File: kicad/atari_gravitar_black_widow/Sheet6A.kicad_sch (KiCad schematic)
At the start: 10 parts

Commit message: All digital done!
Need ground flood and analog section.
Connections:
- net PR82: now also H_8.1 (C)
- net ~{LATCH1}: no longer H_8.1 (C)
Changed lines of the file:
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@@
   (junction (at 174.625 68.58) (diameter 0) (color 0 0 0 0)
   )
-  (junction (at 215.265 205.74) (diameter 0) (color 0 0 0 0)
-  )
   (junction (at 384.81 179.705) (diameter 0) (color 0 0 0 0)
   )
@@
   )
   (junction (at 381.635 182.88) (diameter 0) (color 0 0 0 0)
+  )
+  (junction (at 262.255 205.74) (diameter 0) (color 0 0 0 0)
   )
   (junction (at 170.815 55.88) (diameter 0) (color 0 0 0 0)
@@
     (stroke (width 0) (type default) (color 0 0 0 0))
   )
-  (wire (pts (xy 215.265 205.74) (xy 239.395 205.74))
-    (stroke (width 0) (type default) (color 0 0 0 0))
-  )
   (wire (pts (xy 219.075 226.06) (xy 158.115 226.06))
     (stroke (width 0) (type default) (color 0 0 0 0))
@@
     (stroke (width 0) (type default) (color 0 0 0 0))
   )
+  (wire (pts (xy 262.255 205.74) (xy 262.255 208.28))
+    (stroke (width 0) (type default) (color 0 0 0 0))
+  )
   (wire (pts (xy 236.855 203.2) (xy 236.855 198.12))
     (stroke (width 0) (type default) (color 0 0 0 0))
@@
     (stroke (width 0) (type default) (color 0 0 0 0))
   )
-  (wire (pts (xy 215.265 205.74) (xy 215.265 254.635))
+  (wire (pts (xy 215.265 154.94) (xy 215.265 254.635))
     (stroke (width 0) (type default) (color 0 0 0 0))
   )
@@
     (stroke (width 0) (type default) (color 0 0 0 0))
   )
-  (wire (pts (xy 262.255 157.48) (xy 262.255 208.28))
-    (stroke (width 0) (type default) (color 0 0 0 0))
-  )
   (wire (pts (xy 212.725 101.6) (xy 236.855 101.6))
     (stroke (width 0) (type default) (color 0 0 0 0))
@@
     (stroke (width 0) (type default) (color 0 0 0 0))
   )
+  (wire (pts (xy 262.255 157.48) (xy 262.255 205.74))
+    (stroke (width 0) (type default) (color 0 0 0 0))
+  )
   (wire (pts (xy 154.305 231.14) (xy 154.305 180.34))
     (stroke (width 0) (type default) (color 0 0 0 0))
@@
     (stroke (width 0) (type default) (color 0 0 0 0))
   )
-  (wire (pts (xy 215.265 154.94) (xy 215.265 205.74))
-    (stroke (width 0) (type default) (color 0 0 0 0))
-  )
   (wire (pts (xy 156.21 177.8) (xy 219.075 177.8))
     (stroke (width 0) (type default) (color 0 0 0 0))
@@
     (stroke (width 0) (type default) (color 0 0 0 0))
   )
+  (wire (pts (xy 239.395 205.74) (xy 262.255 205.74))
+    (stroke (width 0) (type default) (color 0 0 0 0))
+  )

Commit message: Fixed various issues and generated gerber files
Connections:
- net ~{ENORM}: now also E_7.4; no longer E_7.5
- net ~{LATCH1}: now also E_7.5; no longer E_7.4
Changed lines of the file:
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@@
     (pin "1")
   )
-  (symbol (lib_name "LS00_1") (lib_id "atari_grav_bw:LS00") (at 194.31 157.48 0) (mirror x) (unit 2) (convert 2)
+  (symbol (lib_id "atari_grav_bw:LS00") (at 194.31 157.48 0) (unit 2) (convert 2)
     (in_bom yes) (on_board yes)
-    (property "Reference" "E_7" (id 0) (at 194.31 158.115 0))
-    (property "Value" "S00" (id 1) (at 194.31 156.21 0))
+    (property "Reference" "E_7" (id 0) (at 194.31 156.845 0))
+    (property "Value" "S00" (id 1) (at 194.31 158.75 0))
     (property "Footprint" "Star_Wars_Vector_PCB:DIP14" (id 2) (at 194.31 157.48 0)
       (effects (font (size 1.27 1.27)) hide)

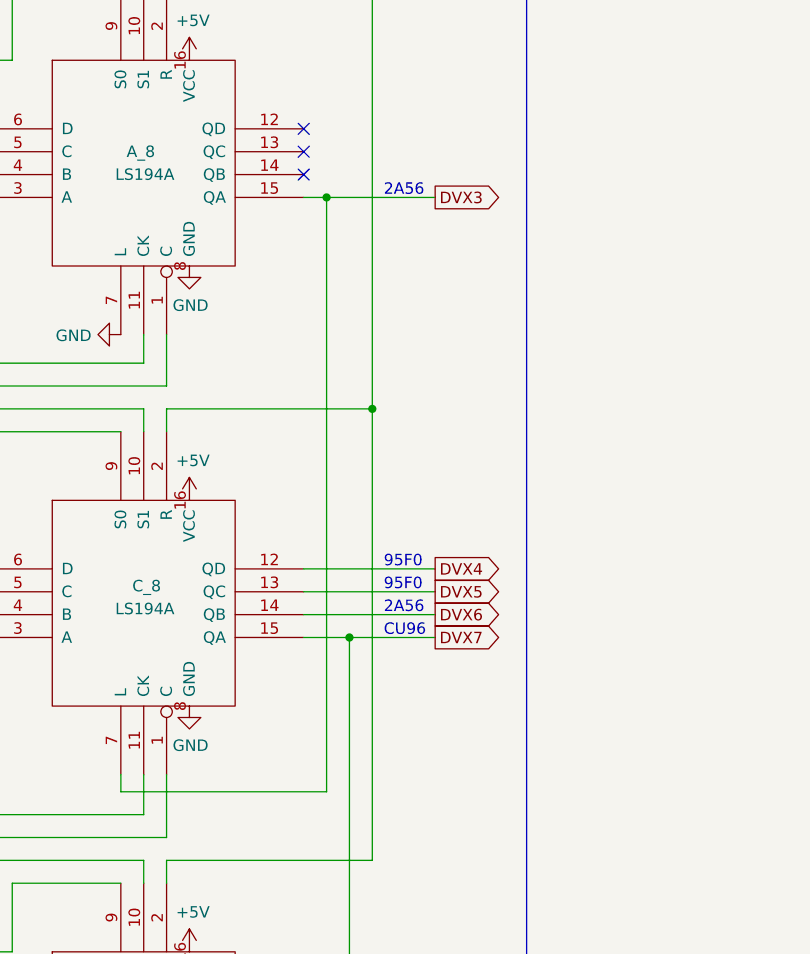
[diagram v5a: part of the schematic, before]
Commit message: caps polarity, c39, c38, transistors holes to .125 mil
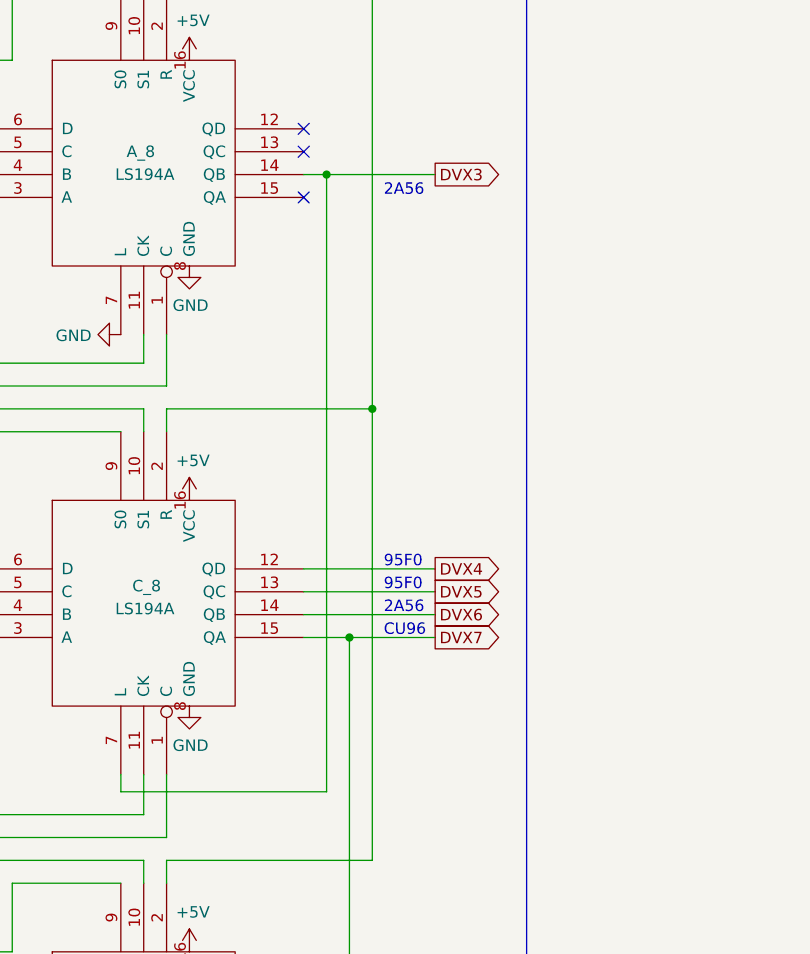
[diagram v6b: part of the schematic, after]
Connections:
- net DVX3: now also A_8.14 (QB); no longer A_8.15 (QA)
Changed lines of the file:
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@@
   (junction (at 215.265 356.235) (diameter 0) (color 0 0 0 0)
   )
+  (junction (at 257.175 231.14) (diameter 0) (color 0 0 0 0)
+  )
   (junction (at 212.725 203.2) (diameter 0) (color 0 0 0 0)
   )
@@
   )
   (junction (at 163.83 127) (diameter 0) (color 0 0 0 0)
-  )
-  (junction (at 257.175 233.68) (diameter 0) (color 0 0 0 0)
   )
   (junction (at 210.185 208.28) (diameter 0) (color 0 0 0 0)
@@
   (no_connect (at 254.635 228.6))
   (no_connect (at 422.275 235.585))
-  (no_connect (at 254.635 231.14))
+  (no_connect (at 254.635 233.68))
   (wire (pts (xy 154.305 81.28) (xy 154.305 180.34))
     (stroke (width 0) (type default) (color 0 0 0 0))
@@
     (stroke (width 0) (type default) (color 0 0 0 0))
   )
-  (wire (pts (xy 257.175 299.72) (xy 257.175 233.68))
+  (wire (pts (xy 257.175 299.72) (xy 257.175 231.14))
     (stroke (width 0) (type default) (color 0 0 0 0))
   )
@@
     (stroke (width 0) (type default) (color 0 0 0 0))
   )
-  (wire (pts (xy 257.175 233.68) (xy 269.24 233.68))
-    (stroke (width 0) (type default) (color 0 0 0 0))
-  )
   (wire (pts (xy 174.625 167.64) (xy 174.625 160.02))
     (stroke (width 0) (type default) (color 0 0 0 0))
@@
     (stroke (width 0) (type default) (color 0 0 0 0))
   )
+  (wire (pts (xy 254.635 231.14) (xy 257.175 231.14))
+    (stroke (width 0) (type default) (color 0 0 0 0))
+  )
   (wire (pts (xy 393.7 213.995) (xy 401.955 213.995))
     (stroke (width 0) (type default) (color 0 0 0 0))
@@
     (stroke (width 0) (type default) (color 0 0 0 0))
   )
+  (wire (pts (xy 257.175 231.14) (xy 269.24 231.14))
+    (stroke (width 0) (type default) (color 0 0 0 0))
+  )
   (wire (pts (xy 152.4 332.74) (xy 219.075 332.74))
     (stroke (width 0) (type default) (color 0 0 0 0))
@@
   )
   (wire (pts (xy 170.815 154.94) (xy 179.07 154.94))
-    (stroke (width 0) (type default) (color 0 0 0 0))
-  )
-  (wire (pts (xy 254.635 233.68) (xy 257.175 233.68))
     (stroke (width 0) (type default) (color 0 0 0 0))
   )
@@
     )
   )
-  (global_label "DVX3" (shape output) (at 269.24 233.68 0) (fields_autoplaced)
-    (effects (font (size 1.27 1.27)) (justify left))
-    (property "Intersheet References" "${INTERSHEET_REFS}" (id 0) (at 0 0 0)
-      (effects (font (size 1.27 1.27)) hide)
-    )
+  (global_label "DVX3" (shape output) (at 269.24 231.14 0) (fields_autoplaced)
+    (effects (font (size 1.27 1.27)) (justify left))
+    (property "Intersheet References" "${INTERSHEET_REFS}" (id 0) (at 0 -2.54 0)
+      (effects (font (size 1.27 1.27)) hide)
+    )

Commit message: Fixed schematic and PCB errors. Added BOM
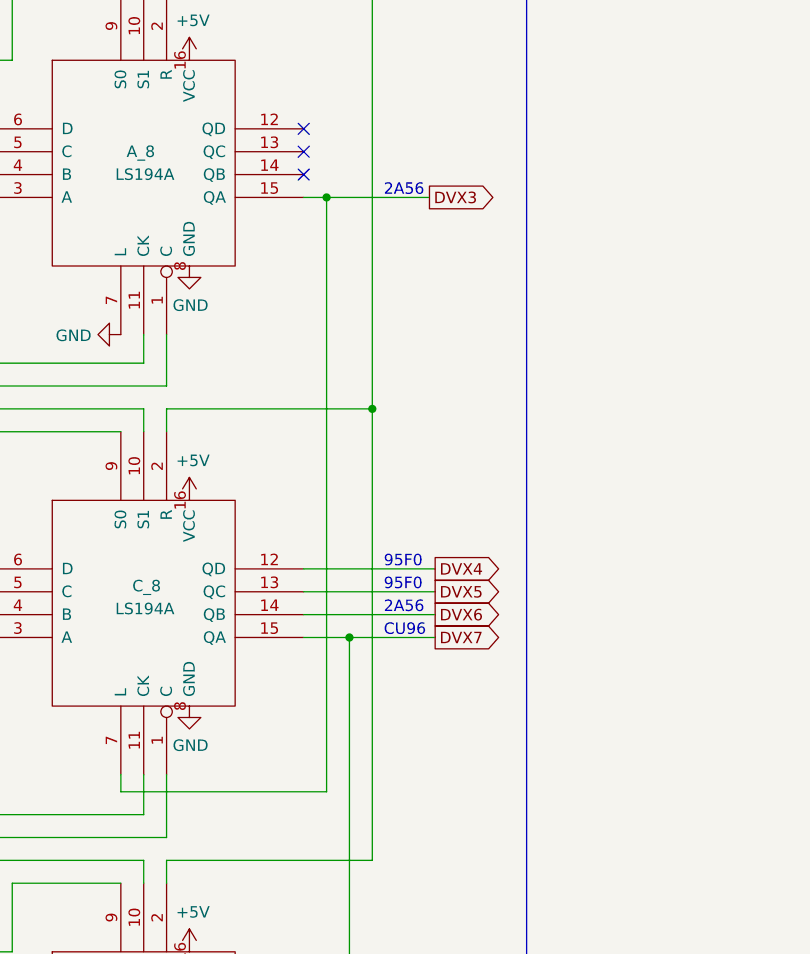
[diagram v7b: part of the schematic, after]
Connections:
- net DVX3: now also A_8.15 (QA); no longer A_8.14 (QB)
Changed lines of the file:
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@@
   (junction (at 215.265 356.235) (diameter 0) (color 0 0 0 0)
   )
-  (junction (at 257.175 231.14) (diameter 0) (color 0 0 0 0)
-  )
   (junction (at 212.725 203.2) (diameter 0) (color 0 0 0 0)
   )
@@
   )
   (junction (at 156.21 78.74) (diameter 0) (color 0 0 0 0)
+  )
+  (junction (at 257.175 233.68) (diameter 0) (color 0 0 0 0)
   )
   (junction (at 152.4 182.88) (diameter 0) (color 0 0 0 0)
@@
   (no_connect (at 254.635 228.6))
   (no_connect (at 422.275 235.585))
-  (no_connect (at 254.635 233.68))
+  (no_connect (at 254.635 231.14))
   (wire (pts (xy 154.305 81.28) (xy 154.305 180.34))
     (stroke (width 0) (type default) (color 0 0 0 0))
@@
     (stroke (width 0) (type default) (color 0 0 0 0))
   )
+  (wire (pts (xy 254.635 233.68) (xy 257.175 233.68))
+    (stroke (width 0) (type default) (color 0 0 0 0))
+  )
   (wire (pts (xy 429.895 238.125) (xy 422.275 238.125))
     (stroke (width 0) (type default) (color 0 0 0 0))
@@
     (stroke (width 0) (type default) (color 0 0 0 0))
   )
-  (wire (pts (xy 257.175 299.72) (xy 257.175 231.14))
+  (wire (pts (xy 257.175 299.72) (xy 257.175 233.68))
     (stroke (width 0) (type default) (color 0 0 0 0))
   )
@@
     (stroke (width 0) (type default) (color 0 0 0 0))
   )
+  (wire (pts (xy 257.175 233.68) (xy 268.605 233.68))
+    (stroke (width 0) (type default) (color 0 0 0 0))
+  )
   (wire (pts (xy 236.855 353.06) (xy 212.725 353.06))
     (stroke (width 0) (type default) (color 0 0 0 0))
@@
     (stroke (width 0) (type default) (color 0 0 0 0))
   )
-  (wire (pts (xy 254.635 231.14) (xy 257.175 231.14))
-    (stroke (width 0) (type default) (color 0 0 0 0))
-  )
   (wire (pts (xy 393.7 213.995) (xy 401.955 213.995))
     (stroke (width 0) (type default) (color 0 0 0 0))
@@
   )
   (wire (pts (xy 222.25 68.58) (xy 222.25 60.96))
-    (stroke (width 0) (type default) (color 0 0 0 0))
-  )
-  (wire (pts (xy 257.175 231.14) (xy 269.24 231.14))
     (stroke (width 0) (type default) (color 0 0 0 0))
   )
@@
     )
   )
-  (global_label "DVX3" (shape output) (at 269.24 231.14 0) (fields_autoplaced)
-    (effects (font (size 1.27 1.27)) (justify left))
-    (property "Intersheet References" "${INTERSHEET_REFS}" (id 0) (at 0 -2.54 0)
-      (effects (font (size 1.27 1.27)) hide)
-    )
+  (global_label "DVX3" (shape output) (at 268.605 233.68 0) (fields_autoplaced)
+    (effects (font (size 1.27 1.27)) (justify left))
+    (property "Intersheet References" "${INTERSHEET_REFS}" (id 0) (at -0.635 0 0)
+      (effects (font (size 1.27 1.27)) hide)
+    )
